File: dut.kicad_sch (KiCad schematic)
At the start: 73 parts, among them J10 Conn_01x20, J11 Conn_01x20, J12 Conn_01x20, J15 Conn_01x20, J2 Conn_01x08, J4 Conn_01x10, J5 Conn_01x20, J6 Conn_01x20, J7 Conn_01x20, J8 Conn_01x02, J9 Conn_01x06

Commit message: where I'm at. fault not needed
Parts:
- removed R71, R72: R_Protect, symbol Device:R_Small
- added R100, R101, R102, R103, R104, R105, R106, R107, R108, R109, R110, R111, R112, R113, R74, R75, R76, R77, R78, R79, R80, R81, R82, R83, R84, R85, R86, R87, R88, R89, R90, R91, R92, R93, R94, R95, R96, R97, R98, R99: 2.2K, Resistor_SMD:R_0402_1005Metric, symbol Device:R_Small
- added R73: 100k, Resistor_SMD:R_0402_1005Metric, symbol Device:R_Small
- J8: footprint (none) -> Connector_PinHeader_2.54mm:PinHeader_1x02_P2.54mm_Vertical
- R14, R15, R35, R36, R37, R38, R39, R40, R41, R42, R43, R44, R45, R46, R47, R48, R49, R50, R51, R52, R53, R54, R55, R56, R57, R58, R59, R60, R61, R62, R63, R64, R65, R66, R67, R68, R69, R70, R8, R9: footprint (none) -> Resistor_SMD:R_0402_1005Metric
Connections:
- net ARDUINO_IOREF is gone; now on net T11: J8.1 (Pin_1)
- net ARDUINO_RESET is gone; now on net T12: J8.2 (Pin_2)
- net B1: now also J5.1 (Pin_1), J9.6 (Pin_6), R51.2, R94.2
- net B10: now also J5.10 (Pin_10), R60.2, R103.2
- net B11: now also J5.11 (Pin_11), R61.2, R104.2
- net B12: now also J5.12 (Pin_12), R62.2, R105.2
- net B13: now also J5.13 (Pin_13), R63.2, R106.2
- net B14: now also J5.14 (Pin_14), J9.1 (Pin_1), R64.2, R107.2
- net B15: now also J5.15 (Pin_15), R65.2, R108.2
- net B16: now also J5.16 (Pin_16), R66.2, R109.2
- net B17: now also J5.17 (Pin_17), R67.2, R110.2
- net B18: now also J5.18 (Pin_18), R68.2, R111.2
- net B19: now also J5.19 (Pin_19), R69.2, R112.2
- net B2: now also J5.2 (Pin_2), J9.5 (Pin_5), R52.2, R95.2
- net B20: now also J5.20 (Pin_20), R70.2, R113.2
- net B3: now also J5.3 (Pin_3), J9.4 (Pin_4), R53.2, R96.2
- net B4: now also J5.4 (Pin_4), J9.3 (Pin_3), R54.2, R97.2
- net B5: now also J5.5 (Pin_5), J9.2 (Pin_2), R55.2, R98.2
- net B6: now also J5.6 (Pin_6), R56.2, R99.2
- net B7: now also J5.7 (Pin_7), R57.2, R100.2
- net B8: now also J5.8 (Pin_8), R58.2, R101.2
- net B9: now also J5.9 (Pin_9), R59.2, R102.2
- net MAX_VOLTAGE: now also R73.1
- net T1: now also J10.1 (Pin_1), J11.1 (Pin_1), J12.1 (Pin_1), J15.1 (Pin_1), J4.1 (Pin_1), J6.1 (Pin_1), J7.1 (Pin_1), R8.1, R74.2
- net T10: now also J10.10 (Pin_10), J11.10 (Pin_10), J12.10 (Pin_10), J15.10 (Pin_10), J4.10 (Pin_10), J6.10 (Pin_10), J7.10 (Pin_10), R40.1, R83.2
- net T11: now also J10.11 (Pin_11), J11.11 (Pin_11), J12.11 (Pin_11), J15.11 (Pin_11), J6.11 (Pin_11), J7.11 (Pin_11), R41.1, R84.2
- net T12: now also J10.12 (Pin_12), J11.12 (Pin_12), J12.12 (Pin_12), J15.12 (Pin_12), J6.12 (Pin_12), J7.12 (Pin_12), R42.1, R85.2
- net T13: now also J10.13 (Pin_13), J11.13 (Pin_13), J12.13 (Pin_13), J15.13 (Pin_13), J2.1 (Pin_1), J6.13 (Pin_13), J7.13 (Pin_13), R43.1, R86.2
- net T14: now also J10.14 (Pin_14), J11.14 (Pin_14), J12.14 (Pin_14), J15.14 (Pin_14), J2.2 (Pin_2), J6.14 (Pin_14), J7.14 (Pin_14), R44.1, R87.2
- net T15: now also J10.15 (Pin_15), J11.15 (Pin_15), J12.15 (Pin_15), J15.15 (Pin_15), J2.3 (Pin_3), J6.15 (Pin_15), J7.15 (Pin_15), R45.1, R88.2
- net T16: now also J10.16 (Pin_16), J11.16 (Pin_16), J12.16 (Pin_16), J15.16 (Pin_16), J2.4 (Pin_4), J6.16 (Pin_16), J7.16 (Pin_16), R46.1, R89.2
- net T17: now also J10.17 (Pin_17), J11.17 (Pin_17), J12.17 (Pin_17), J15.17 (Pin_17), J2.5 (Pin_5), J6.17 (Pin_17), J7.17 (Pin_17), R47.1, R90.2
- net T18: now also J10.18 (Pin_18), J11.18 (Pin_18), J12.18 (Pin_18), J15.18 (Pin_18), J2.6 (Pin_6), J6.18 (Pin_18), J7.18 (Pin_18), R48.1, R91.2
- net T19: now also J10.19 (Pin_19), J11.19 (Pin_19), J12.19 (Pin_19), J15.19 (Pin_19), J2.7 (Pin_7), J6.19 (Pin_19), J7.19 (Pin_19), R49.1, R92.2
- net T2: now also J10.2 (Pin_2), J11.2 (Pin_2), J12.2 (Pin_2), J15.2 (Pin_2), J4.2 (Pin_2), J6.2 (Pin_2), J7.2 (Pin_2), R9.1, R75.2
- net T20: now also J10.20 (Pin_20), J11.20 (Pin_20), J12.20 (Pin_20), J15.20 (Pin_20), J2.8 (Pin_8), J6.20 (Pin_20), J7.20 (Pin_20), R50.1, R93.2
- net T3: now also J10.3 (Pin_3), J11.3 (Pin_3), J12.3 (Pin_3), J15.3 (Pin_3), J4.3 (Pin_3), J6.3 (Pin_3), J7.3 (Pin_3), R14.1, R76.2
- net T4: now also J10.4 (Pin_4), J11.4 (Pin_4), J12.4 (Pin_4), J15.4 (Pin_4), J4.4 (Pin_4), J6.4 (Pin_4), J7.4 (Pin_4), R15.1, R77.2
- net T5: now also J10.5 (Pin_5), J11.5 (Pin_5), J12.5 (Pin_5), J15.5 (Pin_5), J4.5 (Pin_5), J6.5 (Pin_5), J7.5 (Pin_5), R35.1, R78.2
- net T6: now also J10.6 (Pin_6), J11.6 (Pin_6), J12.6 (Pin_6), J15.6 (Pin_6), J4.6 (Pin_6), J6.6 (Pin_6), J7.6 (Pin_6), R36.1, R79.2
- net T7: now also J10.7 (Pin_7), J11.7 (Pin_7), J12.7 (Pin_7), J15.7 (Pin_7), J4.7 (Pin_7), J6.7 (Pin_7), J7.7 (Pin_7), R37.1, R80.2
- net T8: now also J10.8 (Pin_8), J11.8 (Pin_8), J12.8 (Pin_8), J15.8 (Pin_8), J4.8 (Pin_8), J6.8 (Pin_8), J7.8 (Pin_8), R38.1, R81.2
- net T9: now also J10.9 (Pin_9), J11.9 (Pin_9), J12.9 (Pin_9), J15.9 (Pin_9), J4.9 (Pin_9), J6.9 (Pin_9), J7.9 (Pin_9), R39.1, R82.2
- new net GND: R73.2
- new net I2C_PULL_UP: R100.1, R101.1, R102.1, R103.1, R104.1, R105.1, R106.1, R107.1, R108.1, R109.1, R110.1, R111.1, R112.1, R113.1, R74.1, R75.1, R76.1, R77.1, R78.1, R79.1, R80.1, R81.1, R82.1, R83.1, R84.1, R85.1, R86.1, R87.1, R88.1, R89.1, R90.1, R91.1, R92.1, R93.1, R94.1, R95.1, R96.1, R97.1, R98.1, R99.1
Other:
- moved on the sheet: R14, R15, R35, R36, R37, R38, R39, R40, R41, R42, R43, R44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

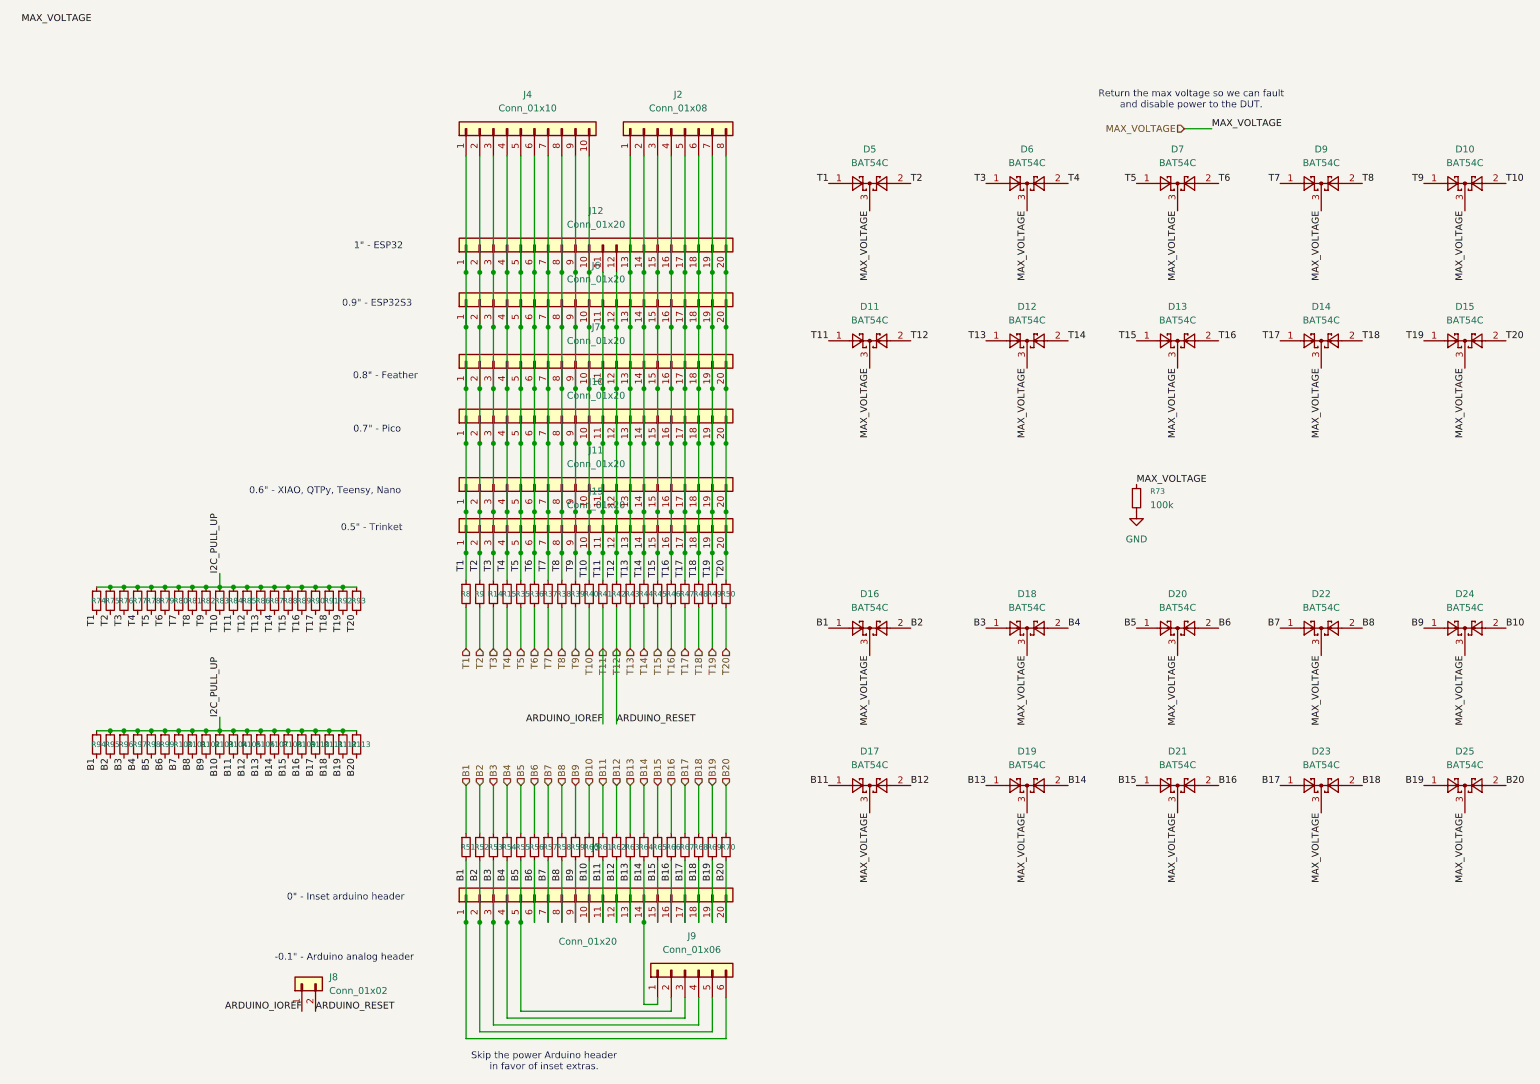
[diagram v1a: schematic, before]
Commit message: Remove fault stuff
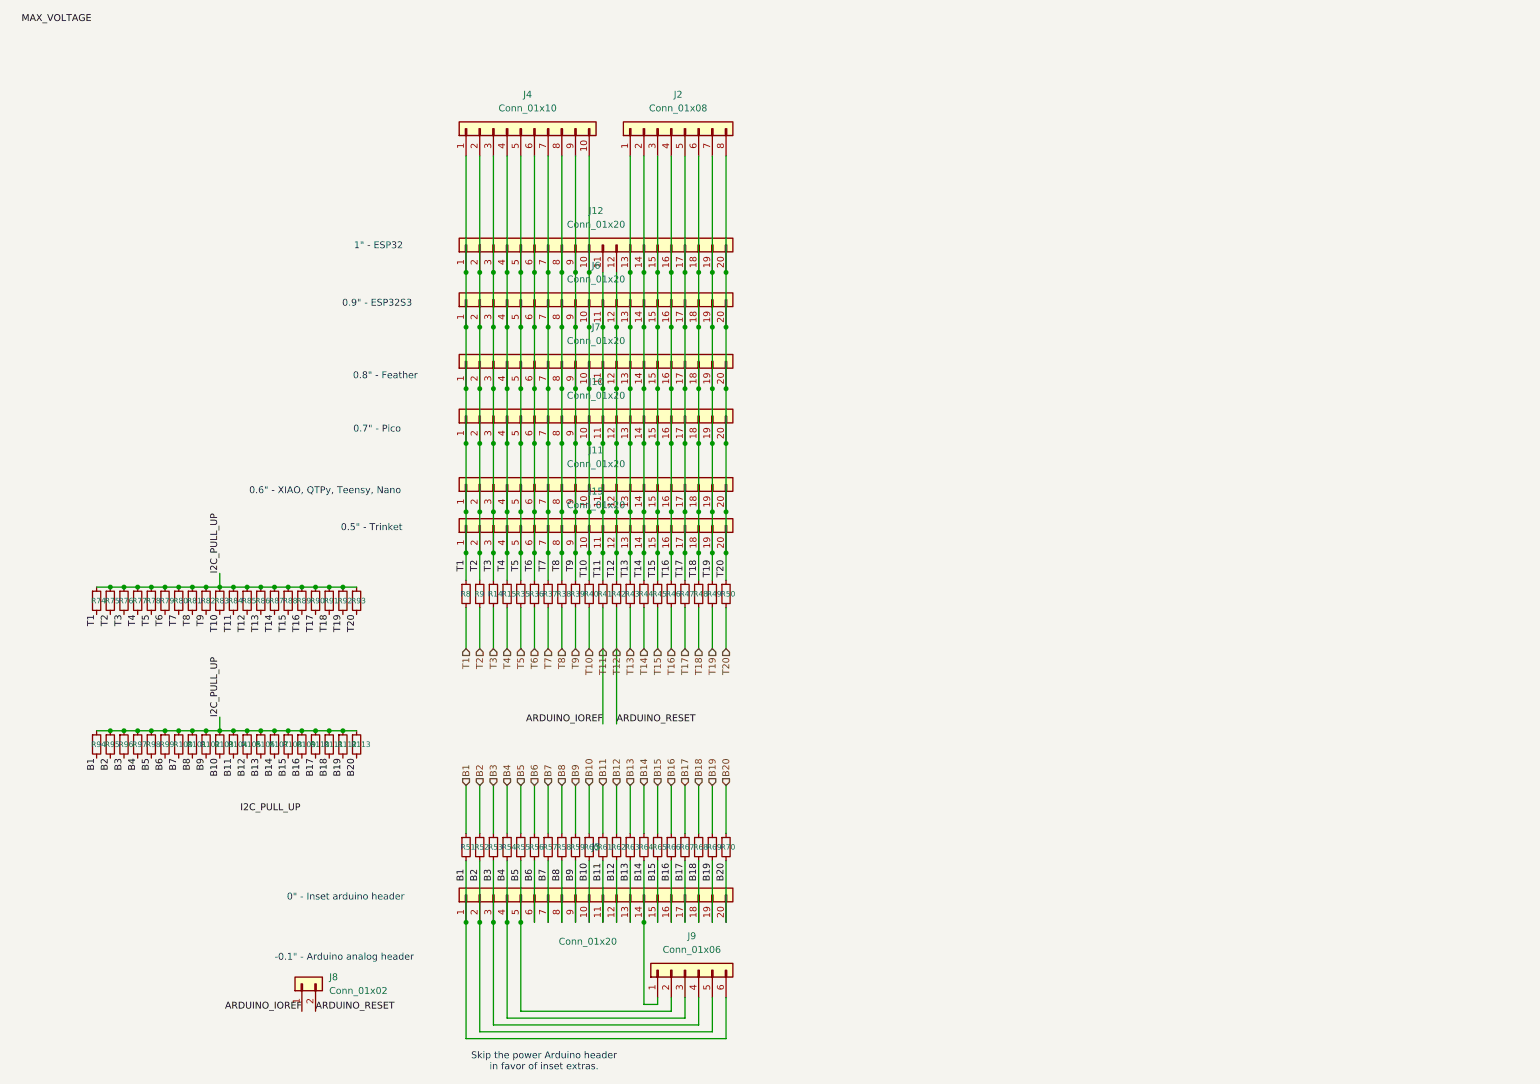
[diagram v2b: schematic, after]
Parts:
- removed D10, D11, D12, D13, D14, D15, D16, D17, D18, D19, D20, D21, D22, D23, D24, D25, D5, D6, D7, D9: BAT54C, Package_TO_SOT_SMD:SOT-23, symbol Diode:BAT54C
- removed R73: 100k, Resistor_SMD:R_0402_1005Metric, symbol Device:R_Small
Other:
- note removed: "Return the max voltage so we can fault and disable power to the DUT."

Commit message: Pack things in
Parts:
- added C58, C59: 10uF, Capacitor_SMD:C_0603_1608Metric, symbol Device:C_Small
- added R71, R72: 10K, Resistor_SMD:R_0402_1005Metric, symbol Device:R_Small
- added U11: MT9700_SY6280, Package_TO_SOT_SMD:SOT-23-5, symbol GenericJLC:MT9700_SY6280
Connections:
- net B1: no longer J5.1 (Pin_1), J9.6 (Pin_6), R51.2, R94.2
- net B10: no longer J5.10 (Pin_10), R103.2, R60.2
- net B11: no longer J5.11 (Pin_11), R104.2, R61.2
- net B12: no longer J5.12 (Pin_12), R105.2, R62.2
- net B13: no longer J5.13 (Pin_13), R106.2, R63.2
- net B14: no longer J5.14 (Pin_14), J9.1 (Pin_1), R107.2, R64.2
- net B15: no longer J5.15 (Pin_15), R108.2, R65.2
- net B16: no longer J5.16 (Pin_16), R109.2, R66.2
- net B17: no longer J5.17 (Pin_17), R110.2, R67.2
- net B18: no longer J5.18 (Pin_18), R111.2, R68.2
- net B19: no longer J5.19 (Pin_19), R112.2, R69.2
- net B2: no longer J5.2 (Pin_2), J9.5 (Pin_5), R52.2, R95.2
- net B20: no longer J5.20 (Pin_20), R113.2, R70.2
- net B3: no longer J5.3 (Pin_3), J9.4 (Pin_4), R53.2, R96.2
- net B4: no longer J5.4 (Pin_4), J9.3 (Pin_3), R54.2, R97.2
- net B5: no longer J5.5 (Pin_5), J9.2 (Pin_2), R55.2, R98.2
- net B6: no longer J5.6 (Pin_6), R56.2, R99.2
- net B7: no longer J5.7 (Pin_7), R100.2, R57.2
- net B8: no longer J5.8 (Pin_8), R101.2, R58.2
- net B9: no longer J5.9 (Pin_9), R102.2, R59.2
- net I2C_PULL_UP: now also C59.1, U11.1 (OUT)
- new net: R72.1, U11.3 (SET)
- new net +3.3V: C58.1, U11.5 (IN)
- new net B10i: J5.10 (Pin_10), R103.2, R60.2
- new net B11i: J5.11 (Pin_11), R104.2, R61.2
- new net B12i: J5.12 (Pin_12), R105.2, R62.2
- new net B13i: J5.13 (Pin_13), R106.2, R63.2
- new net B14i: J5.14 (Pin_14), J9.1 (Pin_1), R107.2, R64.2
- new net B15i: J5.15 (Pin_15), R108.2, R65.2
- new net B16i: J5.16 (Pin_16), R109.2, R66.2
- new net B17i: J5.17 (Pin_17), R110.2, R67.2
- new net B18i: J5.18 (Pin_18), R111.2, R68.2
- new net B19i: J5.19 (Pin_19), R112.2, R69.2
- new net B1i: J5.1 (Pin_1), J9.6 (Pin_6), R51.2, R94.2
- new net B20i: J5.20 (Pin_20), R113.2, R70.2
- new net B2i: J5.2 (Pin_2), J9.5 (Pin_5), R52.2, R95.2
- new net B3i: J5.3 (Pin_3), J9.4 (Pin_4), R53.2, R96.2
- new net B4i: J5.4 (Pin_4), J9.3 (Pin_3), R54.2, R97.2
- new net B5i: J5.5 (Pin_5), J9.2 (Pin_2), R55.2, R98.2
- new net B6i: J5.6 (Pin_6), R56.2, R99.2
- new net B7i: J5.7 (Pin_7), R100.2, R57.2
- new net B8i: J5.8 (Pin_8), R101.2, R58.2
- new net B9i: J5.9 (Pin_9), R102.2, R59.2
- new net ENABLE_I2C_PULLS: R71.1, U11.4 (ON)
- new net GND: C58.2, C59.2, R71.2, R72.2, U11.2 (GND)
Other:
- note added: "6.8k/10k = 0.6A"

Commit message: Drop T20'
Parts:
- removed R50: R_Protect, Resistor_SMD:R_0402_1005Metric, symbol Device:R_Small
- removed R93: 2.2K, Resistor_SMD:R_0402_1005Metric, symbol Device:R_Small
- J10, J11, J12, J15, J6, J7: symbol Connector_Generic:Conn_01x20 -> Connector_Generic:Conn_01x19
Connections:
- net T1: no longer J10.1 (Pin_1), J11.1 (Pin_1), J12.1 (Pin_1), J15.1 (Pin_1), J4.1 (Pin_1), J6.1 (Pin_1), J7.1 (Pin_1), R74.2, R8.1
- net T10: now also J8.1 (Pin_1); no longer J10.10 (Pin_10), J11.10 (Pin_10), J12.10 (Pin_10), J15.10 (Pin_10), J4.10 (Pin_10), J6.10 (Pin_10), J7.10 (Pin_10), R40.1, R83.2
- net T11: now also J8.2 (Pin_2); no longer J10.11 (Pin_11), J11.11 (Pin_11), J12.11 (Pin_11), J15.11 (Pin_11), J6.11 (Pin_11), J7.11 (Pin_11), J8.1 (Pin_1), R41.1, R84.2
- net T12: no longer J10.12 (Pin_12), J11.12 (Pin_12), J12.12 (Pin_12), J15.12 (Pin_12), J6.12 (Pin_12), J7.12 (Pin_12), J8.2 (Pin_2), R42.1, R85.2
- net T13: no longer J10.13 (Pin_13), J11.13 (Pin_13), J12.13 (Pin_13), J15.13 (Pin_13), J2.1 (Pin_1), J6.13 (Pin_13), J7.13 (Pin_13), R43.1, R86.2
- net T14: no longer J10.14 (Pin_14), J11.14 (Pin_14), J12.14 (Pin_14), J15.14 (Pin_14), J2.2 (Pin_2), J6.14 (Pin_14), J7.14 (Pin_14), R44.1, R87.2
- net T15: no longer J10.15 (Pin_15), J11.15 (Pin_15), J12.15 (Pin_15), J15.15 (Pin_15), J2.3 (Pin_3), J6.15 (Pin_15), J7.15 (Pin_15), R45.1, R88.2
- net T16: no longer J10.16 (Pin_16), J11.16 (Pin_16), J12.16 (Pin_16), J15.16 (Pin_16), J2.4 (Pin_4), J6.16 (Pin_16), J7.16 (Pin_16), R46.1, R89.2
- net T17: no longer J10.17 (Pin_17), J11.17 (Pin_17), J12.17 (Pin_17), J15.17 (Pin_17), J2.5 (Pin_5), J6.17 (Pin_17), J7.17 (Pin_17), R47.1, R90.2
- net T18: no longer J10.18 (Pin_18), J11.18 (Pin_18), J12.18 (Pin_18), J15.18 (Pin_18), J2.6 (Pin_6), J6.18 (Pin_18), J7.18 (Pin_18), R48.1, R91.2
- net T19: no longer J10.19 (Pin_19), J11.19 (Pin_19), J12.19 (Pin_19), J15.19 (Pin_19), J2.7 (Pin_7), J6.19 (Pin_19), J7.19 (Pin_19), R49.1, R92.2
- net T2: no longer J10.2 (Pin_2), J11.2 (Pin_2), J12.2 (Pin_2), J15.2 (Pin_2), J4.2 (Pin_2), J6.2 (Pin_2), J7.2 (Pin_2), R75.2, R9.1
- net T3: no longer J10.3 (Pin_3), J11.3 (Pin_3), J12.3 (Pin_3), J15.3 (Pin_3), J4.3 (Pin_3), J6.3 (Pin_3), J7.3 (Pin_3), R14.1, R76.2
- net T4: no longer J10.4 (Pin_4), J11.4 (Pin_4), J12.4 (Pin_4), J15.4 (Pin_4), J4.4 (Pin_4), J6.4 (Pin_4), J7.4 (Pin_4), R15.1, R77.2
- net T5: no longer J10.5 (Pin_5), J11.5 (Pin_5), J12.5 (Pin_5), J15.5 (Pin_5), J4.5 (Pin_5), J6.5 (Pin_5), J7.5 (Pin_5), R35.1, R78.2
- net T6: no longer J10.6 (Pin_6), J11.6 (Pin_6), J12.6 (Pin_6), J15.6 (Pin_6), J4.6 (Pin_6), J6.6 (Pin_6), J7.6 (Pin_6), R36.1, R79.2
- net T7: no longer J10.7 (Pin_7), J11.7 (Pin_7), J12.7 (Pin_7), J15.7 (Pin_7), J4.7 (Pin_7), J6.7 (Pin_7), J7.7 (Pin_7), R37.1, R80.2
- net T8: no longer J10.8 (Pin_8), J11.8 (Pin_8), J12.8 (Pin_8), J15.8 (Pin_8), J4.8 (Pin_8), J6.8 (Pin_8), J7.8 (Pin_8), R38.1, R81.2
- net T9: no longer J10.9 (Pin_9), J11.9 (Pin_9), J12.9 (Pin_9), J15.9 (Pin_9), J4.9 (Pin_9), J6.9 (Pin_9), J7.9 (Pin_9), R39.1, R82.2
- removed net T20: J10.20 (Pin_20), J11.20 (Pin_20), J12.20 (Pin_20), J15.20 (Pin_20), J2.8 (Pin_8), J6.20 (Pin_20), J7.20 (Pin_20)
- new net T10i: J10.10 (Pin_10), J11.10 (Pin_10), J12.10 (Pin_10), J15.10 (Pin_10), J6.10 (Pin_10), J7.10 (Pin_10), R40.1, R83.2
- new net T11i: J10.11 (Pin_11), J11.11 (Pin_11), J12.11 (Pin_11), J15.11 (Pin_11), J6.11 (Pin_11), J7.11 (Pin_11), R41.1, R84.2
- new net T12i: J10.12 (Pin_12), J11.12 (Pin_12), J12.12 (Pin_12), J15.12 (Pin_12), J2.1 (Pin_1), J6.12 (Pin_12), J7.12 (Pin_12), R42.1, R85.2
- new net T13i: J10.13 (Pin_13), J11.13 (Pin_13), J12.13 (Pin_13), J15.13 (Pin_13), J2.2 (Pin_2), J6.13 (Pin_13), J7.13 (Pin_13), R43.1, R86.2
- new net T14i: J10.14 (Pin_14), J11.14 (Pin_14), J12.14 (Pin_14), J15.14 (Pin_14), J2.3 (Pin_3), J6.14 (Pin_14), J7.14 (Pin_14), R44.1, R87.2
- new net T15i: J10.15 (Pin_15), J11.15 (Pin_15), J12.15 (Pin_15), J15.15 (Pin_15), J2.4 (Pin_4), J6.15 (Pin_15), J7.15 (Pin_15), R45.1, R88.2
- new net T16i: J10.16 (Pin_16), J11.16 (Pin_16), J12.16 (Pin_16), J15.16 (Pin_16), J2.5 (Pin_5), J6.16 (Pin_16), J7.16 (Pin_16), R46.1, R89.2
- new net T17i: J10.17 (Pin_17), J11.17 (Pin_17), J12.17 (Pin_17), J15.17 (Pin_17), J2.6 (Pin_6), J6.17 (Pin_17), J7.17 (Pin_17), R47.1, R90.2
- new net T18i: J10.18 (Pin_18), J11.18 (Pin_18), J12.18 (Pin_18), J15.18 (Pin_18), J2.7 (Pin_7), J6.18 (Pin_18), J7.18 (Pin_18), R48.1, R91.2
- new net T19i: J10.19 (Pin_19), J11.19 (Pin_19), J12.19 (Pin_19), J15.19 (Pin_19), J2.8 (Pin_8), J6.19 (Pin_19), J7.19 (Pin_19), R49.1, R92.2
- new net T1i: J10.1 (Pin_1), J11.1 (Pin_1), J12.1 (Pin_1), J15.1 (Pin_1), J4.1 (Pin_1), J6.1 (Pin_1), J7.1 (Pin_1), R74.2, R8.1
- new net T2i: J10.2 (Pin_2), J11.2 (Pin_2), J12.2 (Pin_2), J15.2 (Pin_2), J4.2 (Pin_2), J6.2 (Pin_2), J7.2 (Pin_2), R75.2, R9.1
- new net T3i: J10.3 (Pin_3), J11.3 (Pin_3), J12.3 (Pin_3), J15.3 (Pin_3), J4.3 (Pin_3), J6.3 (Pin_3), J7.3 (Pin_3), R14.1, R76.2
- new net T4i: J10.4 (Pin_4), J11.4 (Pin_4), J12.4 (Pin_4), J15.4 (Pin_4), J4.5 (Pin_5), J6.4 (Pin_4), J7.4 (Pin_4), R15.1, R77.2
- new net T5i: J10.5 (Pin_5), J11.5 (Pin_5), J12.5 (Pin_5), J15.5 (Pin_5), J4.6 (Pin_6), J6.5 (Pin_5), J7.5 (Pin_5), R35.1, R78.2
- new net T6i: J10.6 (Pin_6), J11.6 (Pin_6), J12.6 (Pin_6), J15.6 (Pin_6), J4.7 (Pin_7), J6.6 (Pin_6), J7.6 (Pin_6), R36.1, R79.2
- new net T7i: J10.7 (Pin_7), J11.7 (Pin_7), J12.7 (Pin_7), J15.7 (Pin_7), J4.8 (Pin_8), J6.7 (Pin_7), J7.7 (Pin_7), R37.1, R80.2
- new net T8i: J10.8 (Pin_8), J11.8 (Pin_8), J12.8 (Pin_8), J15.8 (Pin_8), J4.9 (Pin_9), J6.8 (Pin_8), J7.8 (Pin_8), R38.1, R81.2
- new net T9i: J10.9 (Pin_9), J11.9 (Pin_9), J12.9 (Pin_9), J15.9 (Pin_9), J4.10 (Pin_10), J6.9 (Pin_9), J7.9 (Pin_9), R39.1, R82.2
- no-connect marks 0 -> 1
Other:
- note added: "GND"

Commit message: Swirly gridify
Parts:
- J10, J11, J12, J6, J7: footprint Connector_PinHeader_2.54mm:PinHeader_1x20_P2.54mm_Vertical -> Connector_PinHeader_2.54mm:PinHeader_1x19_P2.54mm_Vertical
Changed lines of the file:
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@@
 			)
 		)
-		(property "Footprint" "Connector_PinHeader_2.54mm:PinHeader_1x20_P2.54mm_Vertical"
+		(property "Footprint" "Connector_PinHeader_2.54mm:PinHeader_1x19_P2.54mm_Vertical"
 			(at 105.41 74.93 0)
 			(hide yes)
@@
 			)
 		)
-		(property "Footprint" "Connector_PinHeader_2.54mm:PinHeader_1x20_P2.54mm_Vertical"
+		(property "Footprint" "Connector_PinHeader_2.54mm:PinHeader_1x19_P2.54mm_Vertical"
 			(at 105.41 53.34 0)
 			(hide yes)
@@
 			)
 		)
-		(property "Footprint" "Connector_PinHeader_2.54mm:PinHeader_1x20_P2.54mm_Vertical"
+		(property "Footprint" "Connector_PinHeader_2.54mm:PinHeader_1x19_P2.54mm_Vertical"
 			(at 105.41 43.18 0)
 			(hide yes)
@@
 			)
 		)
-		(property "Footprint" "Connector_PinHeader_2.54mm:PinHeader_1x20_P2.54mm_Vertical"
+		(property "Footprint" "Connector_PinHeader_2.54mm:PinHeader_1x19_P2.54mm_Vertical"
 			(at 105.41 64.77 0)
 			(hide yes)
@@
 			)
 		)
-		(property "Footprint" "Connector_PinHeader_2.54mm:PinHeader_1x20_P2.54mm_Vertical"
+		(property "Footprint" "Connector_PinHeader_2.54mm:PinHeader_1x19_P2.54mm_Vertical"
 			(at 105.41 87.63 0)
 			(hide yes)
